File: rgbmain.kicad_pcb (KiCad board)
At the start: 2 copper layers, 100 x 86 mm, 18 parts, among them J1 Conn_01x10_Pin, J10 Conn_01x04, J2 Conn_01x10_Pin, J3 Conn_01x09_Pin, J4 Conn_01x09, J5 Conn_01x06_Pin, J6 Conn_01x06, J7 Conn_01x13, J8 Conn_01x13, J9 Conn_01x01, M1 MountingHole_6.4mm_M6, M3 MountingHole_4.3mm_M4, M4 MountingHole_4.3mm_M4, Q1 BSS138, U1 Elite-Pi

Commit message: pcb layout complete
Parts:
- moved J3 90.9 mm to (164.0, 85.5), turned to -90 degrees
- moved J4 87.5 mm to (74.0, 98.5), turned to 90 degrees
- moved J9 85.2 mm to (84.0, 129.0)
- moved J1 83.9 mm to (160.9, 72.0), turned to -90 degrees
- moved J2 83.9 mm to (77.0, 72.0), turned to 90 degrees
- moved J7 70.5 mm to (165.7, 140.0)
- moved J8 70.5 mm to (95.2, 140.0)
- moved R1 50.0 mm to (148.0, 118.5), turned to 0 degrees
- moved Q1 47.4 mm to (153.4, 116.0), turned to 0 degrees
- moved R2 42.0 mm to (148.0, 113.5), turned to 0 degrees
- moved J10 37.5 mm to (97.5, 109.0)
- moved J6 20.2 mm to (74.0, 113.5), turned to -90 degrees
- moved J5 20.2 mm to (164.0, 133.7), turned to 90 degrees
- renumbered J8 to J1, J7 to J2, J6 to J3, J5 to J4, J4 to J5, J3 to J6, J2 to J7, J1 to J8
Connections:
- J1 pad 1: unconnected-(J8-Pin_1-Pad1) -> /ROW_F1
- J1 pad 10: unconnected-(J8-Pin_10-Pad10) -> /ROW_F2
- J1 pad 11: unconnected-(J8-Pin_11-Pad11) -> /ROW_F1
- J1 pad 2: unconnected-(J8-Pin_2-Pad2) -> /ROW_F2
- J1 pad 3: unconnected-(J8-Pin_3-Pad3) -> /COL_7
- J1 pad 4: unconnected-(J8-Pin_4-Pad4) -> /COL_7
- J1 pad 5: unconnected-(J8-Pin_5-Pad5) -> /ROW_6
- J1 pad 6: unconnected-(J8-Pin_6-Pad6) -> /COL_5
- J1 pad 7: unconnected-(J8-Pin_7-Pad7) -> /ROW_F2
- J1 pad 8: unconnected-(J8-Pin_8-Pad8) -> /ROW_F1
- J1 pad 9: unconnected-(J8-Pin_9-Pad9) -> /COL_6
- J10 pad 4: /SLC0 -> /SCL0
- J2 pad 10: unconnected-(J7-Pin_10-Pad10) -> /ROW_F2
- J2 pad 11: unconnected-(J7-Pin_11-Pad11) -> /ROW_F1
- J2 pad 12: unconnected-(J7-Pin_12-Pad12) -> /ROW_6
- J2 pad 13: unconnected-(J7-Pin_13-Pad13) -> /COL_2
- J2 pad 3: unconnected-(J7-Pin_3-Pad3) -> /ROW_F2
- J2 pad 4: unconnected-(J7-Pin_4-Pad4) -> /ROW_F1
- J2 pad 6: unconnected-(J7-Pin_6-Pad6) -> /COL_3
- J2 pad 7: unconnected-(J7-Pin_7-Pad7) -> /ROW_F2
- J2 pad 8: unconnected-(J7-Pin_8-Pad8) -> /ROW_F1
- J2 pad 9: unconnected-(J7-Pin_9-Pad9) -> /COL_4
- J4 pad 1: /COL_1 -> /COL_6
- J4 pad 2: /COL_2 -> /COL_5
- J4 pad 3: /COL_3 -> /COL_4
- J4 pad 4: /COL_4 -> /COL_3
- J4 pad 5: /COL_5 -> /COL_2
- J4 pad 6: /COL_6 -> /COL_1
- J5 pad 1: /VSS -> GND
- J5 pad 4: /VDD -> +5V
- J6 pad 1: /VSS -> /ROW_5
- J6 pad 2: /DIN_KEY_LEFT -> /ROW_4
- J6 pad 3: /DOUT_KEY_LEFT -> /ROW_3
- J6 pad 4: /VDD -> /ROW_2
- J6 pad 6: /ROW_2 -> +5V
- J6 pad 7: /ROW_3 -> /DOUT_KEY_LEFT
- J6 pad 8: /ROW_4 -> /DIN_KEY_LEFT
- J6 pad 9: /ROW_5 -> GND
- J7 pad 10: /VDD -> +5V
- J7 pad 3: /ROW_4 -> /ROW_1
- J7 pad 4: /ROW_6 -> /ROW_2
- J7 pad 6: /ROW_7 -> /ROW_6
- J7 pad 9: /VSS -> GND
- J8 pad 1: /ROW_6 -> /ROW_2
- J8 pad 10: /VDD -> +5V
- J8 pad 2: /ROW_7 -> /ROW_6
- J8 pad 3: /ROW_1 -> /ROW_5
- J8 pad 8: /ROW_2 -> /ROW_4
- J8 pad 9: /VSS -> GND
- U1 pad 14: unconnected-(U1-D23-Pad14) -> /ROW_F1
- U1 pad 15: unconnected-(U1-D20-Pad15) -> /ROW_F2
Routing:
- net /ROW_6: track 0.00 -> 255.1 mm, vias 0 -> 1
- net +5V: track 0.00 -> 228.3 mm, vias 0 -> 1
- net GND: track 0.00 -> 224.8 mm, vias 0 -> 2
- net /ROW_F1: track 0.00 -> 186.5 mm, vias 0 -> 1
- net /ROW_F2: track 0.00 -> 183.0 mm, vias 0 -> 1
- net /ROW_2: track 0.00 -> 161.8 mm, vias 0 -> 3
- net /ROW_1: track 0.00 -> 140.2 mm, vias 0 -> 2
- net /ROW_4: track 0.00 -> 138.8 mm, vias 0 -> 2
- net /ROW_3: track 0.00 -> 135.6 mm, vias 0 -> 2
- net /ROW_5: track 0.00 -> 132.4 mm, vias 0 -> 2
- net /COL_14: track 0.00 -> 109.4 mm
- net /COL_13: track 0.00 -> 109.0 mm
- net /COL_6: track 0.00 -> 98.7 mm
- net /COL_5: track 0.00 -> 98.4 mm
- net /DIN_THUMB_LEFT: track 0.00 -> 85.8 mm
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
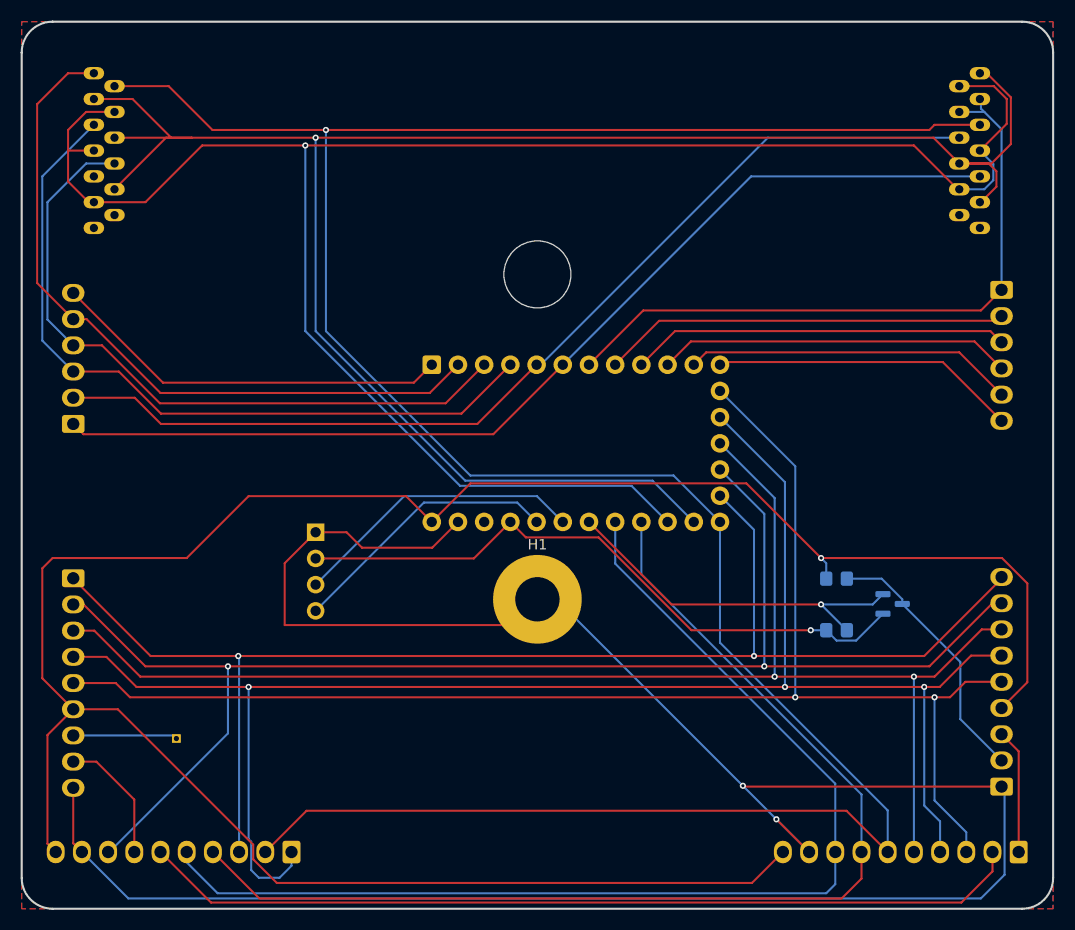
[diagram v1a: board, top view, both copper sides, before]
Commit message: changed thumb connectors
wanted thumbs to be the same as stock.
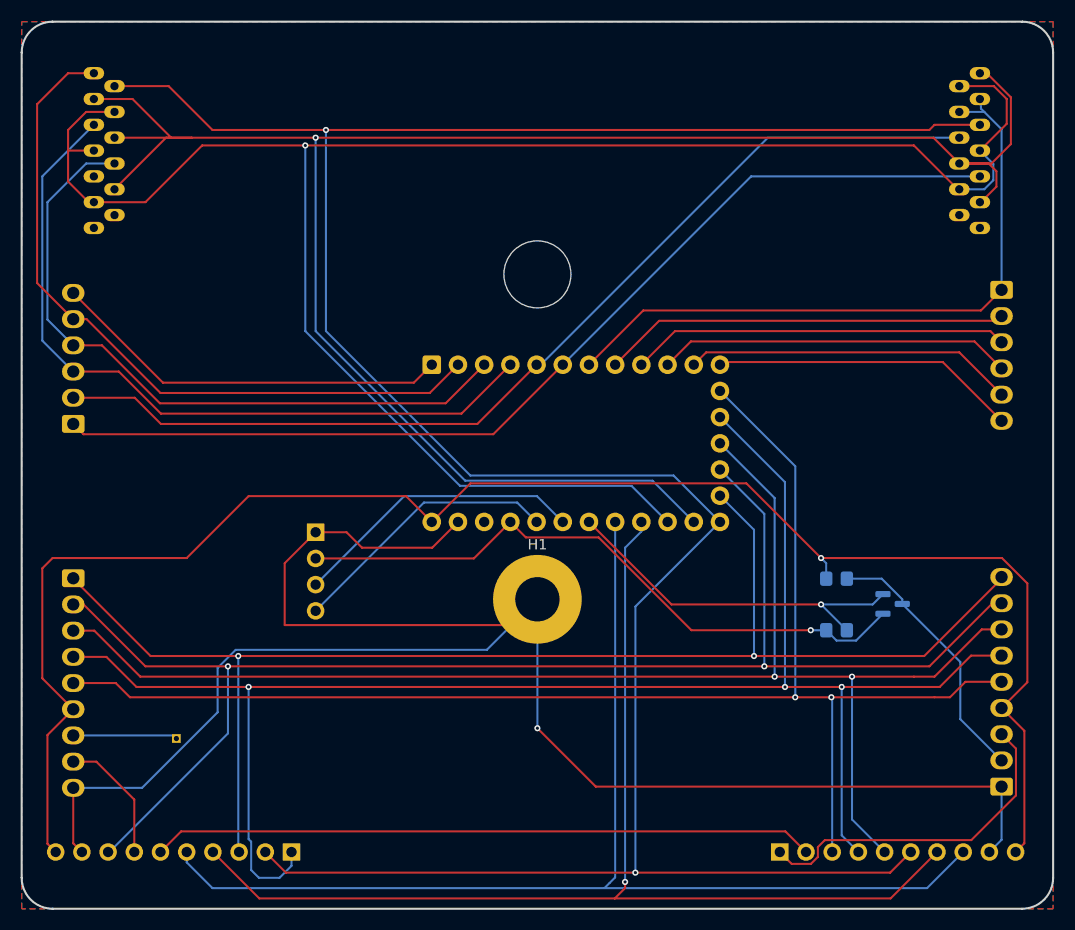
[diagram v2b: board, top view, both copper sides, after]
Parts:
- J7, J8: footprint Connector_Molex:Molex_KK-254_AE-6410-10A_1x10_P2.54mm_Vertical -> Connector_PinHeader_2.54mm:PinHeader_1x10_P2.54mm_Vertical
- moved J7 23.2 mm to (142.5, 140.0), turned to -90 degrees
- turned J8 to 90 degrees
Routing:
- net +5V: track 228.3 -> 165.7 mm
- net GND: track 224.8 -> 180.0 mm, vias 2 -> 1
- net /DIN_THUMB_LEFT: track 85.8 -> 64.2 mm
- net /DIN_THUMB_RIGHT: track 12.1 -> 33.2 mm
- net /COL_14: track 109.4 -> 114.7 mm
- net /COL_13: track 109.0 -> 111.5 mm, vias 0 -> 1
- net /ROW_3: track 135.6 -> 136.9 mm
- net /ROW_1: track 140.2 -> 138.9 mm
- net /ROW_6: track 255.1 -> 254.3 mm, vias 1 -> 2

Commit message: more connector flipping
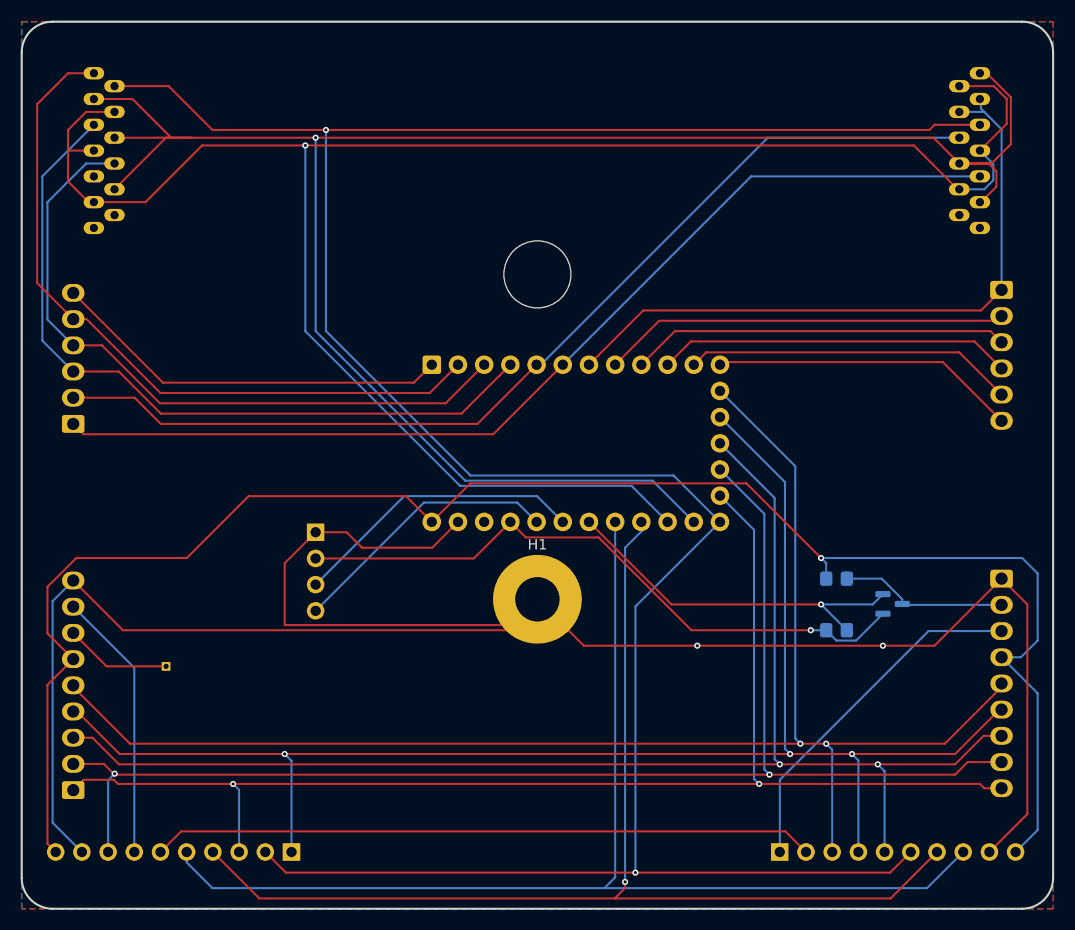
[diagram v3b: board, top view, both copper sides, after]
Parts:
- moved J6 20.5 mm to (74.0, 134.0), turned to 90 degrees
- moved J5 20.2 mm to (164.0, 113.5), turned to -90 degrees
- moved J9 7.07 mm to (83.0, 122.0)
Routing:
- net GND: track 180.0 -> 206.6 mm, vias 1 -> 2
- net /DIN_KEY_LEFT: track 12.5 -> 27.2 mm
- net /ROW_2: track 161.8 -> 148.5 mm
- net /DIN_KEY_RIGHT: track 25.8 -> 17.2 mm
- net /ROW_4: track 138.8 -> 130.5 mm
- net /ROW_1: track 138.9 -> 143.2 mm
- net /ROW_5: track 132.4 -> 128.1 mm
- net +5V: track 165.7 -> 168.0 mm
- net /ROW_3: track 136.9 -> 134.5 mm
- net /DIN_THUMB_RIGHT: track 33.2 -> 34.5 mm
